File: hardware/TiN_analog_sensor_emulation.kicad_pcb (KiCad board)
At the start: 2 copper layers, 100 x 100 mm, 175 parts, among them J1 Conn_02x02_Odd_Even, J2 Conn_01x04_Male, J3 Micro_SD_Card, J4 BOOT0, J5 Conn_01x03_Male, J6 display, J7 Barrel_Jack, J8 Conn_02x08_Odd_Even, SW2 SW_right, SW3 SW_middle2, SW4 SW_top, SW5 SW_middle, SW6 SW_bot, SW7 SW_Left, U1 STM32F042C6Tx, U10 MCP42010, U11 ADA4898-3, U12 ADA4898-3, U13 MCP42010, U14 MCP42010, U15 MCP42050, U16 MCP42050, U17 MCP42050, U18 LT1529CQ#PBF, U19 LT1528CQ, U2 ADA4898-3, U3 ADA4898-3, U4 MCP42010, U5 ADA4898-3, U6 ADA4898-3, U7 MCP42010, U8 ADA4898-3, U9 ADA4898-3, Y1 Crystal_GND24

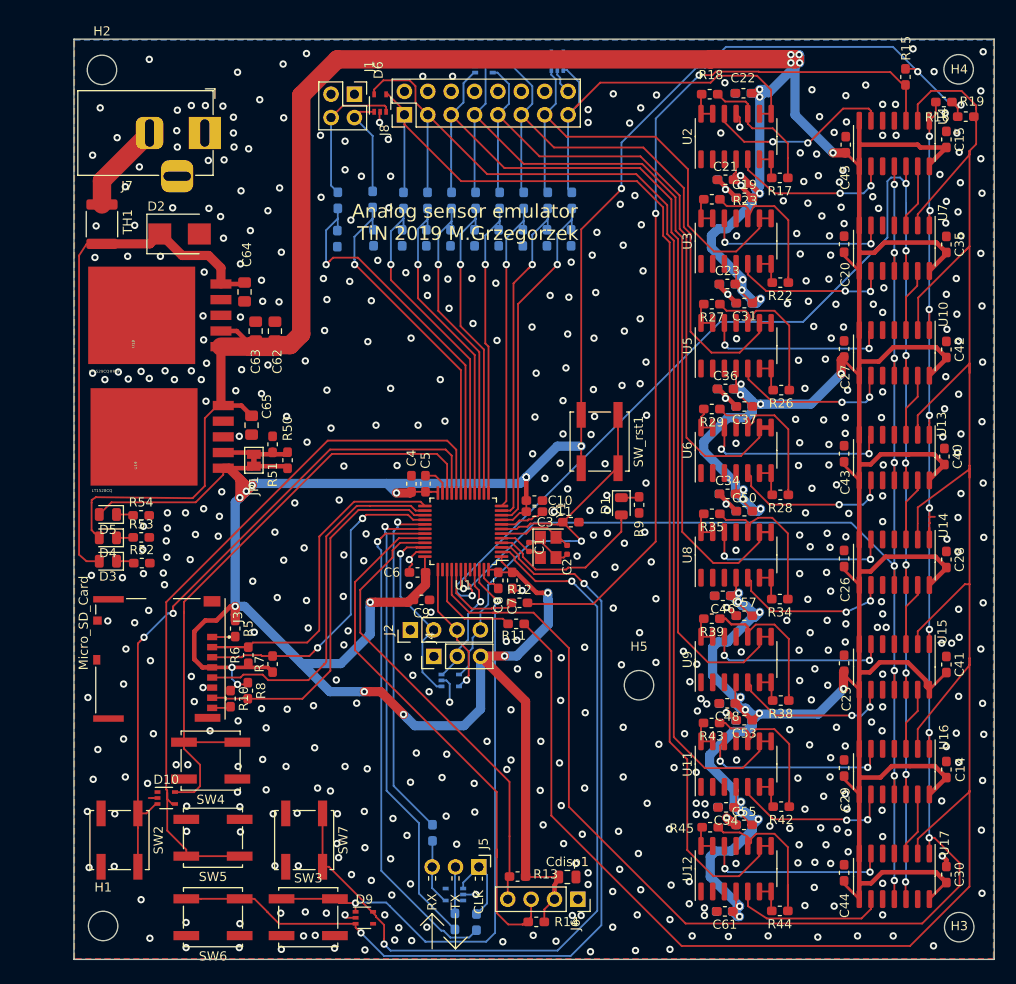
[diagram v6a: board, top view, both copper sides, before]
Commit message: update top overlay, drc przechodzi, dodny shielding wokół ścieżek zegarowych, dodane zdjęcia płytki
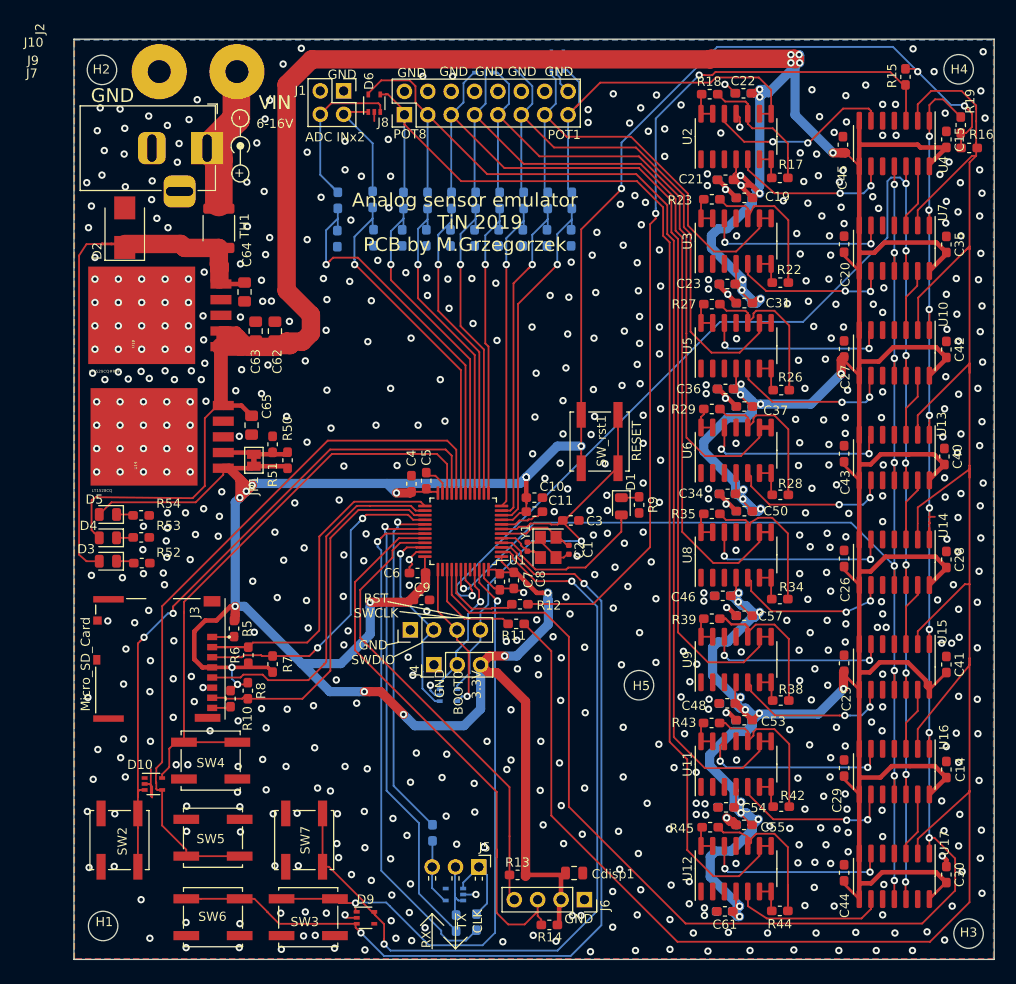
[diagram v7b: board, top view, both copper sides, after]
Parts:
- added J10: Conn_01x01_Male, Connector_Wire:SolderWirePad_1x01_Drill2.5mm, F.Cu at (112.7, 53.5)
- added J9: Conn_01x01_Male, Connector_Wire:SolderWirePad_1x01_Drill2.5mm, F.Cu at (104.3, 53.5)
- added REF**: KiCad-Logo2_5mm_SilkScreen, Symbol:KiCad-Logo2_5mm_SilkScreen, B.Cu at (99.6, 136.8)
- added REF**: Symbol_Barrel_Polarity, Symbol:Symbol_Barrel_Polarity, F.Cu at (113.2, 61.6)
- moved TH1 12.7 mm to (110.7, 70.5)
- moved D2 6.00 mm to (100.5, 70.5), turned to 90 degrees
- moved R16 3.42 mm to (192.3, 61.8)
- moved R19 3.10 mm to (191.4, 59.3), turned to 90 degrees
- moved D10 2.07 mm to (103.6, 130.9)
- moved J7 1.67 mm to (109.5, 61.8)
- moved D7 1.61 mm to (135.7, 121.3)
- moved R14 1.46 mm to (146.7, 146.3)
- moved H3 1.23 mm to (192.2, 147.2)
- moved J1 1.22 mm to (124.3, 55.6)
- moved J4 0.91 mm to (134.1, 118.0)
- moved Cdisp1 0.85 mm to (149.4, 140.6)
- moved J6 0.71 mm to (150.5, 143.5)
- moved D6 0.64 mm to (127.6, 57.0)
- moved C5 0.34 mm to (133.3, 98.0)
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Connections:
- J7 pad 1: GND -> Net-(J10-Pad1)
- J7 pad 2: Net-(J7-Pad2) -> GND
- TH1 pad 2: Net-(J7-Pad2) -> Net-(J10-Pad1)
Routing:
- net Net-(J10-Pad1): track 0.00 -> 16.4 mm
- net +5V: track 588.5 -> 600.0 mm
- net Net-(J7-Pad2): track 9.91 -> 0.00 mm
- net GND: track 52.9 -> 58.9 mm, vias 547 -> 643
- net +3.3VA: track 325.5 -> 329.7 mm
- net /digital_pot/CS: track 188.8 -> 192.9 mm
- net /MCU/sw_top: track 68.5 -> 65.3 mm
- net Net-(D6-Pad3): track 16.0 -> 18.2 mm
- net /MCU/I2C_SCL: track 59.5 -> 61.2 mm
- net /MCU/SWCLK: track 14.9 -> 16.6 mm
- net /MCU/SWDIO: track 20.6 -> 22.2 mm
- net /MCU/~RST: track 46.9 -> 48.5 mm
- net /digital_pot/pot2: track 50.6 -> 49.0 mm
- net /MCU/BOOT0: track 13.7 -> 15.0 mm
- net /MCU/sw_left: track 74.4 -> 73.2 mm
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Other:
- board text added: "+"
- board text added: "-"
- board text added: "3.3V"
- board text added: "6-16V"
- board text added: "ADC INx2"
- board text added: "Analog sensor emulator TiN 2019 PCB by M.Grzegorzek"
- board text added: "BOOT0"
- board text added: "GND"
- board text added: "GND SWDIO"
- board text added: "POT1"
- board text added: "POT8"
- board text added: "RESET"
- board text added: "RST SWCLK"
- board text added: "VIN"
- board text removed: "Analog sensor emulator TiN 2019 M.Grzegorzek"

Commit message: drobne poprawki w przelotkach
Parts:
- moved R7 0.85 mm to (116.3, 117.1)
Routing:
- net +3.3VA: track 329.7 -> 337.2 mm, vias 18 -> 20
- net /MCU/SDCLK: track 39.6 -> 37.0 mm
- net /MCU/SDMISO: track 40.7 -> 38.4 mm
- net /MCU/I2C_SCL: track 61.2 -> 63.3 mm
- net /MCU/SDMOSI: track 35.2 -> 33.3 mm
- net /digital_pot/CS: track 192.9 -> 191.5 mm
- net GND: track 58.9 -> 60.2 mm, vias 643 -> 687
- net /MCU/SD~SS: track 36.0 -> 34.9 mm
- net +5V: track 600.0 -> 601.1 mm
- net /MCU/USART_CK: track 55.6 -> 56.1 mm
- net Net-(U10-Pad3): track 6.95 -> 7.46 mm
